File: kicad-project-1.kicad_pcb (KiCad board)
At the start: 2 copper layers, 10 parts, among them J1 Conn_02x03_Odd_Even, J2 Conn_01x05_Male, U1 Pico-MCU_RaspberryPi_and_Boar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, U2 Pololu_4Ch

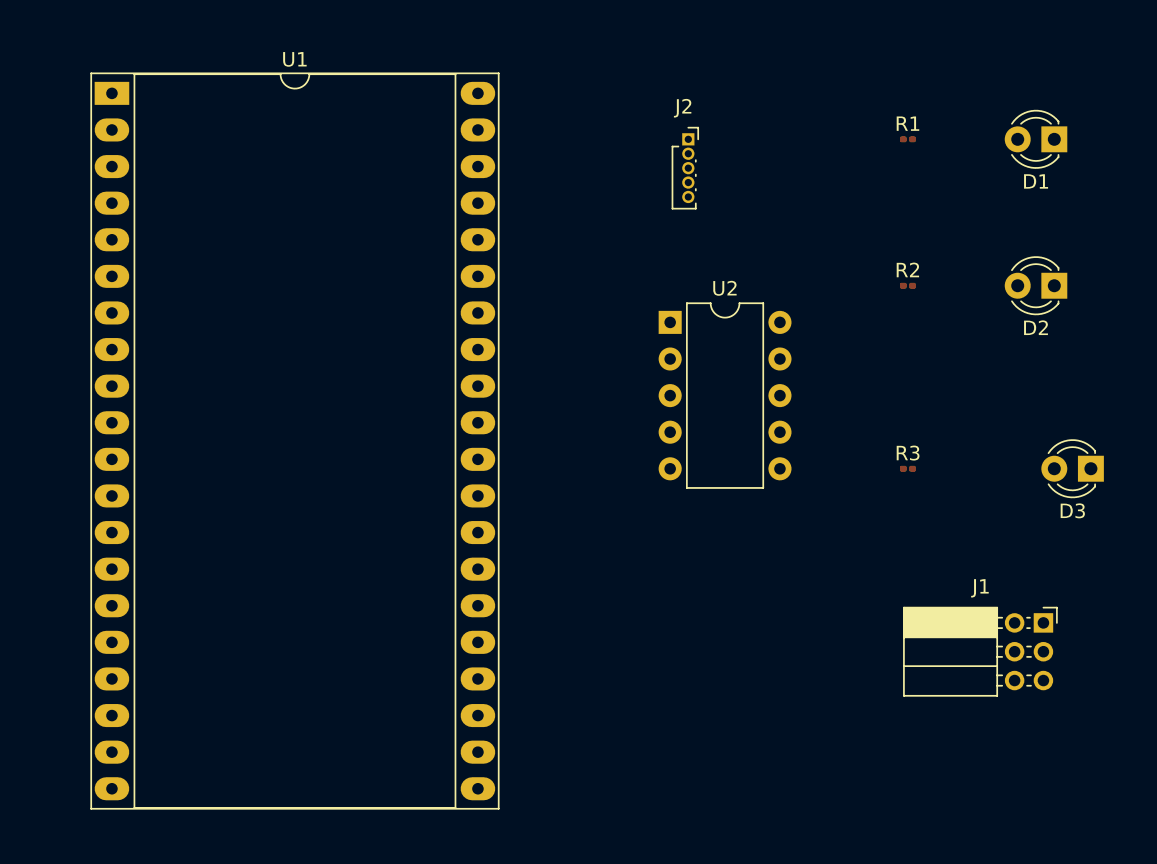
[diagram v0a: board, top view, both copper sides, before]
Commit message: from the pcb exported kicad-project-1.dsn and used java -jar freerouting-1.9.0.jar used kicad-project-1.dsn  and did the routing. Then export Spectra Session file. kicad-project-1.ses This file was imported in kicad pcb
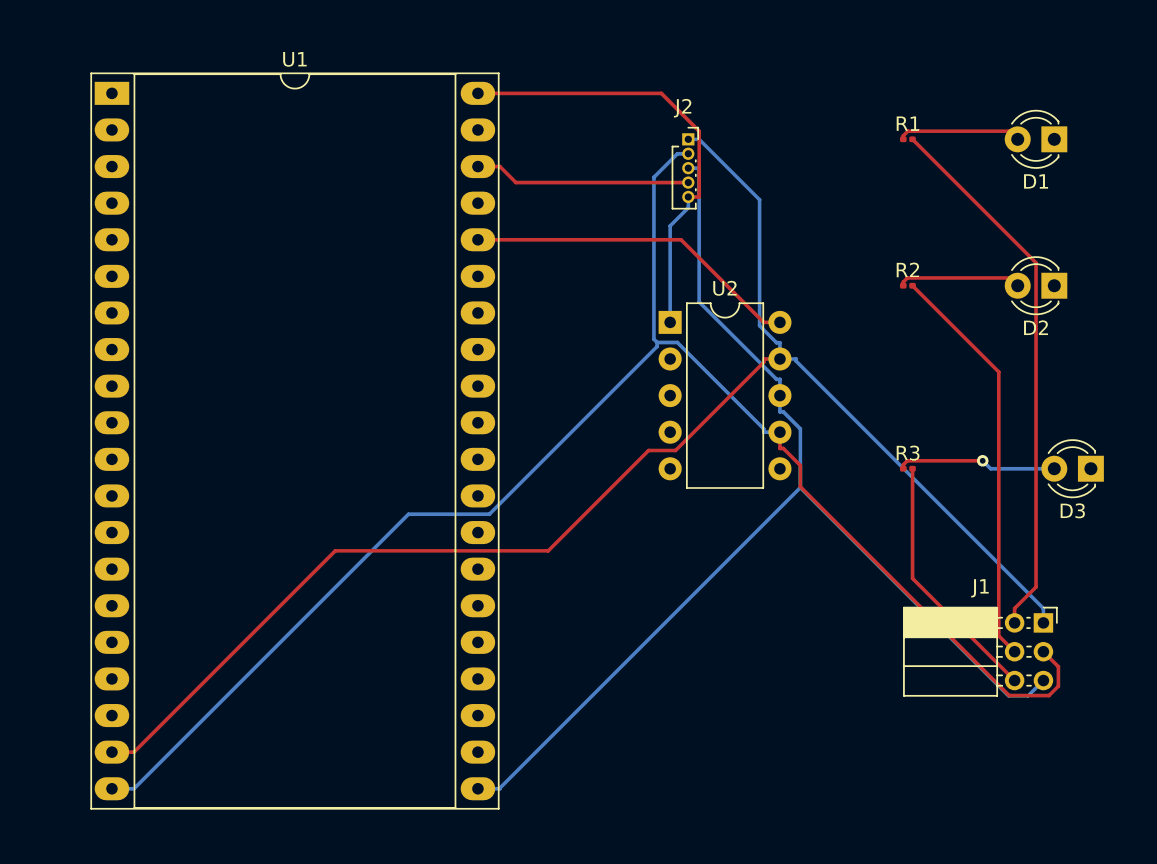
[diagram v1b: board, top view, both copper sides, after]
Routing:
- net Net-(J1-Pad3): track 0.00 -> 108.2 mm
- net Net-(J1-Pad1): track 0.00 -> 102.8 mm
- net Net-(J1-Pad5): track 0.00 -> 80.5 mm
- net Net-(J1-Pad2): track 0.00 -> 37.7 mm
- net Net-(J2-Pad5): track 0.00 -> 31.0 mm
- net Net-(J1-Pad4): track 0.00 -> 28.3 mm
- net Net-(U1-Pad36): track 0.00 -> 23.3 mm
- net Net-(J1-Pad6): track 0.00 -> 17.6 mm
- net Net-(J2-Pad4): track 0.00 -> 15.1 mm
- net Net-(D3-Pad2): track 0.00 -> 11.1 mm, vias 0 -> 1
- net Net-(D1-Pad2): track 0.00 -> 8.55 mm
- net Net-(D2-Pad2): track 0.00 -> 8.54 mm
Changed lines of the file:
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@@
     )
   )
+  (segment (start 144.7819 78.1727) (end 144.46 78.4946) (width 0.25) (layer "F.Cu") (net 2))
+  (segment (start 144.46 78.4946) (end 144.46 78.74) (width 0.25) (layer "F.Cu") (net 2))
+  (segment (start 151.8327 78.1727) (end 144.7819 78.1727) (width 0.25) (layer "F.Cu") (net 2))
+  (segment (start 152.4 78.74) (end 151.8327 78.1727) (width 0.25) (layer "F.Cu") (net 2))
+  (segment (start 144.46 88.6434) (end 144.46 88.9) (width 0.25) (layer "F.Cu") (net 4))
+  (segment (start 151.8629 88.3629) (end 144.7405 88.3629) (width 0.25) (layer "F.Cu") (net 4))
+  (segment (start 152.4 88.9) (end 151.8629 88.3629) (width 0.25) (layer "F.Cu") (net 4))
+  (segment (start 144.7405 88.3629) (end 144.46 88.6434) (width 0.25) (layer "F.Cu") (net 4))
+  (segment (start 144.46 101.6) (end 144.4601 101.6) (width 0.25) (layer "F.Cu") (net 6))
+  (segment (start 144.7355 101.049) (end 149.9693 101.049) (width 0.25) (layer "F.Cu") (net 6))
+  (segment (start 144.4601 101.6) (end 144.4601 101.3244) (width 0.25) (layer "F.Cu") (net 6))
+  (segment (start 144.4601 101.3244) (end 144.7355 101.049) (width 0.25) (layer "F.Cu") (net 6))
+  (via (at 149.9693 101.049) (size 0.8) (drill 0.4) (layers "F.Cu" "B.Cu") (net 6))
+  (segment (start 150.5203 101.6) (end 149.9693 101.049) (width 0.25) (layer "B.Cu") (net 6))
+  (segment (start 154.94 101.6) (end 150.5203 101.6) (width 0.25) (layer "B.Cu") (net 6))
+  (segment (start 134.7731 94.2185) (end 134.7731 93.985) (width 0.25) (layer "F.Cu") (net 7))
+  (segment (start 91.0669 121.27) (end 105.0369 107.3) (width 0.25) (layer "F.Cu") (net 7))
+  (segment (start 128.6566 100.335) (end 134.7731 94.2185) (width 0.25) (layer "F.Cu") (net 7))
+  (segment (start 126.7817 100.335) (end 128.6566 100.335) (width 0.25) (layer "F.Cu") (net 7))
+  (segment (start 119.8167 107.3) (end 126.7817 100.335) (width 0.25) (layer "F.Cu") (net 7))
+  (segment (start 135.9 93.985) (end 134.7731 93.985) (width 0.25) (layer "F.Cu") (net 7))
+  (segment (start 89.54 121.27) (end 91.0669 121.27) (width 0.25) (layer "F.Cu") (net 7))
+  (segment (start 105.0369 107.3) (end 119.8167 107.3) (width 0.25) (layer "F.Cu") (net 7))
+  (segment (start 134.4854 82.9335) (end 134.4854 91.677) (width 0.25) (layer "B.Cu") (net 7))
+  (segment (start 135.6665 92.8581) (end 135.9 92.8581) (width 0.25) (layer "B.Cu") (net 7))
+  (segment (start 137.0269 94.14) (end 137.0269 93.985) (width 0.25) (layer "B.Cu") (net 7))
+  (segment (start 134.4854 91.677) (end 135.6665 92.8581) (width 0.25) (layer "B.Cu") (net 7))
+  (segment (start 154.185 111.2981) (end 137.0269 94.14) (width 0.25) (layer "B.Cu") (net 7))
+  (segment (start 135.9 93.985) (end 135.9 92.8581) (width 0.25) (layer "B.Cu") (net 7))
+  (segment (start 129.54 78.74) (end 130.2919 78.74) (width 0.25) (layer "B.Cu") (net 7))
+  (segment (start 154.185 112.3) (end 154.185 111.2981) (width 0.25) (layer "B.Cu") (net 7))
+  (segment (start 130.2919 78.74) (end 134.4854 82.9335) (width 0.25) (layer "B.Cu") (net 7))
+  (segment (start 135.9 93.985) (end 137.0269 93.985) (width 0.25) (layer "B.Cu") (net 7))
+  (segment (start 152.185 111.2981) (end 153.67 109.8131) (width 0.25) (layer "F.Cu") (net 8))
+  (segment (start 153.67 87.31) (end 145.1 78.74) (width 0.25) (layer "F.Cu") (net 8))
+  (segment (start 152.185 112.3) (end 152.185 111.2981) (width 0.25) (layer "F.Cu") (net 8))
+  (segment (start 153.67 109.8131) (end 153.67 87.31) (width 0.25) (layer "F.Cu") (net 8))
+  (segment (start 135.9 99.065) (end 135.9 100.1919) (width 0.25) (layer "F.Cu") (net 9))
+  (segment (start 151.8044 117.341) (end 137.3146 102.8512) (width 0.25) (layer "F.Cu") (net 9))
+  (segment (start 155.2234 116.6903) (end 154.5727 117.341) (width 0.25) (layer "F.Cu") (net 9))
+  (segment (start 137.3146 101.373) (end 136.1335 100.1919) (width 0.25) (layer "F.Cu") (net 9))
+  (segment (start 154.5727 117.341) (end 151.8044 117.341) (width 0.25) (layer "F.Cu") (net 9))
+  (segment (start 154.185 114.3) (end 155.2234 115.3384) (width 0.25) (layer "F.Cu") (net 9))
+  (segment (start 136.1335 100.1919) (end 135.9 100.1919) (width 0.25) (layer "F.Cu") (net 9))
+  (segment (start 155.2234 115.3384) (end 155.2234 116.6903) (width 0.25) (layer "F.Cu") (net 9))
+  (segment (start 137.3146 102.8512) (end 137.3146 101.373) (width 0.25) (layer "F.Cu") (net 9))
+  (segment (start 110.1169 104.76) (end 115.7324 104.76) (width 0.25) (layer "B.Cu") (net 9))
+  (segment (start 127.1531 92.6108) (end 127.1531 81.375) (width 0.25) (layer "B.Cu") (net 9))
+  (segment (start 127.1531 81.375) (end 128.7881 79.74) (width 0.25) (layer "B.Cu") (net 9))
+  (segment (start 127.3799 92.8376) (end 127.1531 92.6108) (width 0.25) (layer "B.Cu") (net 9))
+  (segment (start 89.54 123.81) (end 91.0669 123.81) (width 0.25) (layer "B.Cu") (net 9))
+  (segment (start 135.9 99.065) (end 134.7731 99.065) (width 0.25) (layer "B.Cu") (net 9))
+  (segment (start 115.7324 104.76) (end 127.3799 93.1125) (width 0.25) (layer "B.Cu") (net 9))
+  (segment (start 134.7731 98.8315) (end 134.7731 99.065) (width 0.25) (layer "B.Cu") (net 9))
+  (segment (start 127.3799 93.1125) (end 127.3799 92.8376) (width 0.25) (layer "B.Cu") (net 9))
+  (segment (start 127.3799 92.8376) (end 128.7792 92.8376) (width 0.25) (layer "B.Cu") (net 9))
+  (segment (start 128.7792 92.8376) (end 134.7731 98.8315) (width 0.25) (layer "B.Cu") (net 9))
+  (segment (start 129.54 79.74) (end 128.7881 79.74) (width 0.25) (layer "B.Cu") (net 9))
+  (segment (start 91.0669 123.81) (end 110.1169 104.76) (width 0.25) (layer "B.Cu") (net 9))
+  (segment (start 151.0855 94.8855) (end 145.1 88.9) (width 0.25) (layer "F.Cu") (net 10))
+  (segment (start 152.185 114.3) (end 151.0855 113.2005) (width 0.25) (layer "F.Cu") (net 10))
+  (segment (start 151.0855 113.2005) (end 151.0855 94.8855) (width 0.25) (layer "F.Cu") (net 10))
+  (segment (start 116.4669 123.7595) (end 116.4669 123.81) (width 0.25) (layer "B.Cu") (net 11))
+  (segment (start 153.1248 117.3602) (end 151.763 117.3602) (width 0.25) (layer "B.Cu") (net 11))
+  (segment (start 135.6665 95.3981) (end 135.9 95.3981) (width 0.25) (layer "B.Cu") (net 11))
+  (segment (start 135.9 96.525) (end 135.9 97.6519) (width 0.25) (layer "B.Cu") (net 11))
+  (segment (start 136.1335 97.6519) (end 135.9 97.6519) (width 0.25) (layer "B.Cu") (net 11))
+  (segment (start 137.3146 98.833) (end 136.1335 97.6519) (width 0.25) (layer "B.Cu") (net 11))
+  (segment (start 154.185 116.3) (end 153.1248 117.3602) (width 0.25) (layer "B.Cu") (net 11))
+  (segment (start 130.2919 90.0235) (end 135.6665 95.3981) (width 0.25) (layer "B.Cu") (net 11))
+  (segment (start 151.763 117.3602) (end 137.3146 102.9118) (width 0.25) (layer "B.Cu") (net 11))
+  (segment (start 135.9 96.525) (end 135.9 95.3981) (width 0.25) (layer "B.Cu") (net 11))
+  (segment (start 129.54 80.74) (end 130.2919 80.74) (width 0.25) (layer "B.Cu") (net 11))
+  (segment (start 137.3146 102.9118) (end 116.4669 123.7595) (width 0.25) (layer "B.Cu") (net 11))
+  (segment (start 130.2919 80.74) (end 130.2919 90.0235) (width 0.25) (layer "B.Cu") (net 11))
+  (segment (start 137.3146 102.9118) (end 137.3146 98.833) (width 0.25) (layer "B.Cu") (net 11))
+  (segment (start 114.94 123.81) (end 116.4669 123.81) (width 0.25) (layer "B.Cu") (net 11))
+  (segment (start 152.185 116.3) (end 145.1 109.215) (width 0.25) (layer "F.Cu") (net 12))
+  (segment (start 145.1 109.215) (end 145.1 101.6) (width 0.25) (layer "F.Cu") (net 12))
+  (segment (start 134.7731 91.445) (end 129.0381 85.71) (width 0.25) (layer "F.Cu") (net 45))
+  (segment (start 135.9 91.445) (end 134.7731 91.445) (width 0.25) (layer "F.Cu") (net 45))
+  (segment (start 129.0381 85.71) (end 114.94 85.71) (width 0.25) (layer "F.Cu") (net 45))
+  (segment (start 114.94 80.63) (end 116.4669 80.63) (width 0.25) (layer "F.Cu") (net 47))
+  (segment (start 117.5769 81.74) (end 116.4669 80.63) (width 0.25) (layer "F.Cu") (net 47))
+  (segment (start 129.54 81.74) (end 117.5769 81.74) (width 0.25) (layer "F.Cu") (net 47))
+  (segment (start 130.2919 78.174) (end 127.6679 75.55) (width 0.25) (layer "F.Cu") (net 49))
+  (segment (start 129.54 82.74) (end 130.2919 82.74) (width 0.25) (layer "F.Cu") (net 49))
+  (segment (start 130.2919 82.74) (end 130.2919 78.174) (width 0.25) (layer "F.Cu") (net 49))
+  (segment (start 127.6679 75.55) (end 114.94 75.55) (width 0.25) (layer "F.Cu") (net 49))
+  (segment (start 129.54 82.74) (end 129.54 83.4919) (width 0.25) (layer "B.Cu") (net 49))
+  (segment (start 128.28 84.7519) (end 128.28 91.445) (width 0.25) (layer "B.Cu") (net 49))
+  (segment (start 129.54 83.4919) (end 128.28 84.7519) (width 0.25) (layer "B.Cu") (net 49))
 )

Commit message: update required
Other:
- board outline added: 76.2 x 55.9 mm
